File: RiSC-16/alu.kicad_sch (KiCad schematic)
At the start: 0 parts

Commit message: Added sheet for register file.
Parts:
- added C1, C2, C3, C4, C5: 0.1 uF, symbol Device:C_Small_US
- added U1: 74LS283, symbol 74xx:74LS283
- added U2: 74LS00, symbol 74xx:74LS00
- added U3, U5: 74LS175, symbol 74xx:74LS175
- added U4: 74LS257, symbol 74xx:74LS257
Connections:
- new net: U1.1 (S2), U4.5 (I0b)
- new net: U1.10 (S4), U4.11 (I0d)
- new net: U1.11 (B4), U2.13, U5.15 (Q3)
- new net: U1.12 (A4), U2.12, U3.15 (Q3)
- new net: U1.13 (S3), U4.14 (I0c)
- new net: U1.14 (A3), U2.9, U3.10 (Q2)
- new net: U1.15 (B3), U2.10, U5.10 (Q2)
- new net: U1.2 (B2), U2.5, U5.7 (Q1)
- new net: U1.3 (A2), U2.4, U3.7 (Q1)
- new net: U1.4 (S1), U4.2 (I0a)
- new net: U1.5 (A1), U2.1, U3.2 (Q0)
- new net: U1.6 (B1), U2.2, U5.2 (Q0)
- new net: U2.11, U4.10 (I1d)
- new net: U2.8, U4.13 (I1c)
- new net: U2.3, U4.3 (I1a)
- new net: U2.6, U4.6 (I1b)
- new net +5V: C1.1, C2.1, C3.1, C4.1, C5.1, U1.16 (VCC), U2.14 (VCC), U3.16 (VCC), U4.16 (VCC), U5.16 (VCC)
- new net ADD/NAND: U4.1 (S)
- new net ALUout: U4.15 (OE)
- new net Ain: U3.9 (Cp)
- new net Bin: U5.9 (Cp)
- new net Cin: U1.7 (C0)
- new net Cout: U1.9 (C4)
- new net GND: C1.2, C2.2, C3.2, C4.2, C5.2, U1.8 (GND), U2.7 (GND), U3.8 (GND), U4.8 (GND), U5.8 (GND)
- new net Reset: U3.1 (~{Mr}), U5.1 (~{Mr})
- new net d0: U3.4 (D0), U4.4 (Za), U5.4 (D0)
- new net d1: U3.5 (D1), U4.7 (Zb), U5.5 (D1)
- new net d2: U3.12 (D2), U4.12 (Zc), U5.12 (D2)
- new net d3: U3.13 (D3), U4.9 (Zd), U5.13 (D3)
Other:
- note added: "ALU 4-bit slice Four required for ALU"

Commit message: First draft of register file.
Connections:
- net d0: no longer U5.4 (D0)
- net d1: no longer U5.5 (D1)
- net d2: no longer U5.12 (D2)
- net d3: no longer U5.13 (D3)
- new net a0: U5.4 (D0)
- new net a1: U5.5 (D1)
- new net a2: U5.12 (D2)
- new net a3: U5.13 (D3)

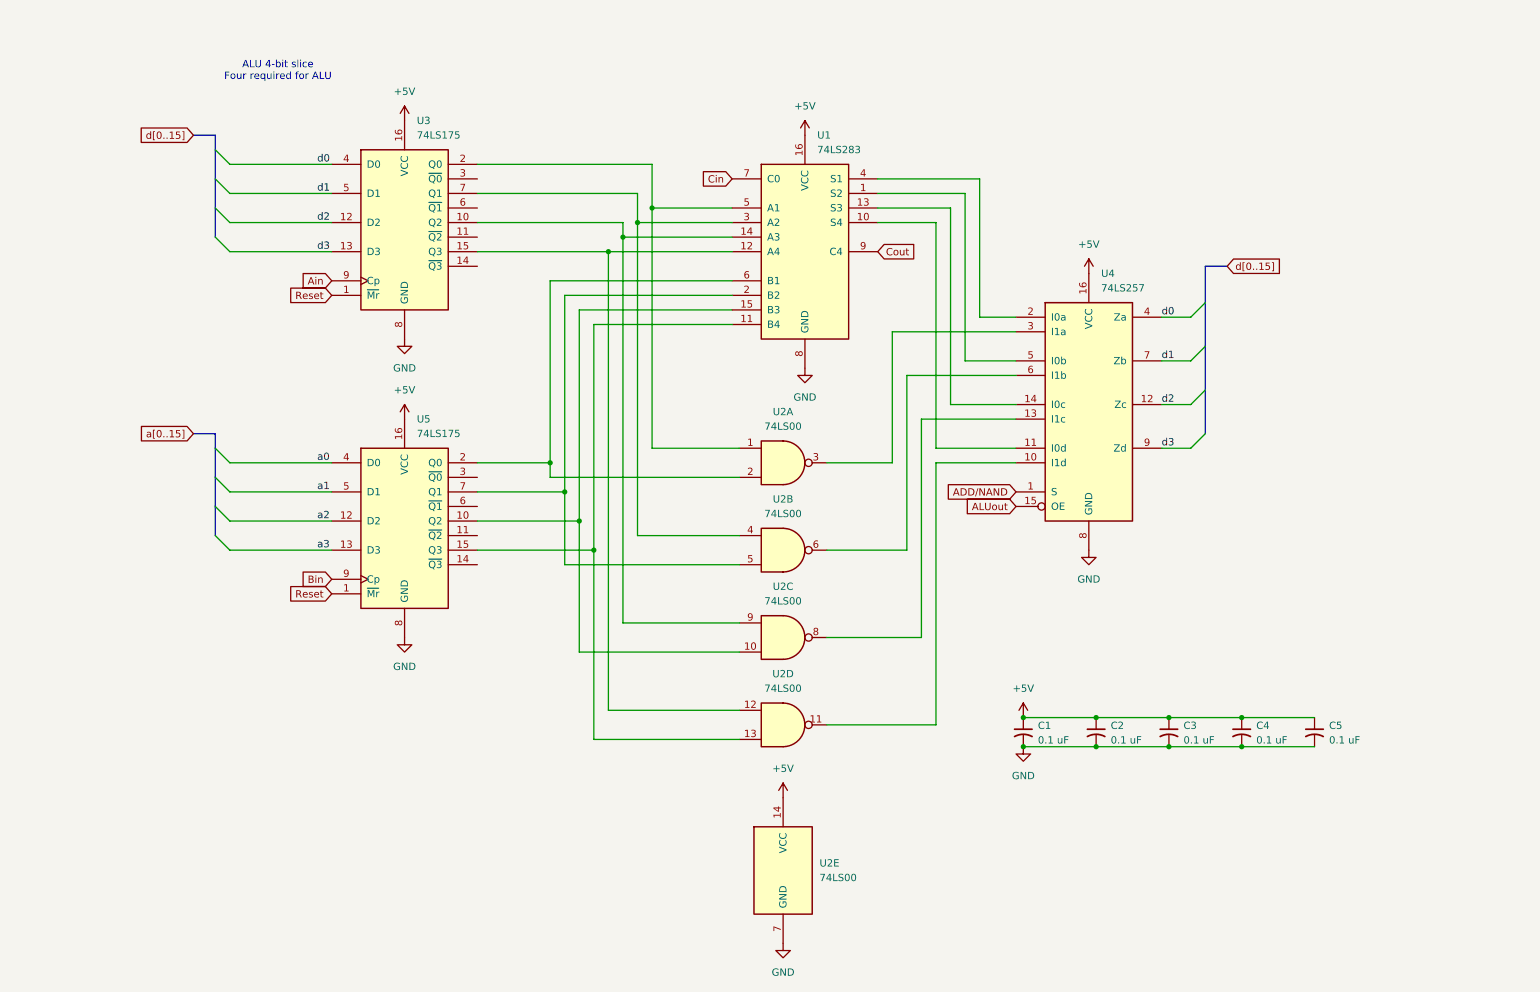
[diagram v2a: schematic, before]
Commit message: Reworked ALU to use 74LS181 and control signals from Pro. Jacob's reference paper.
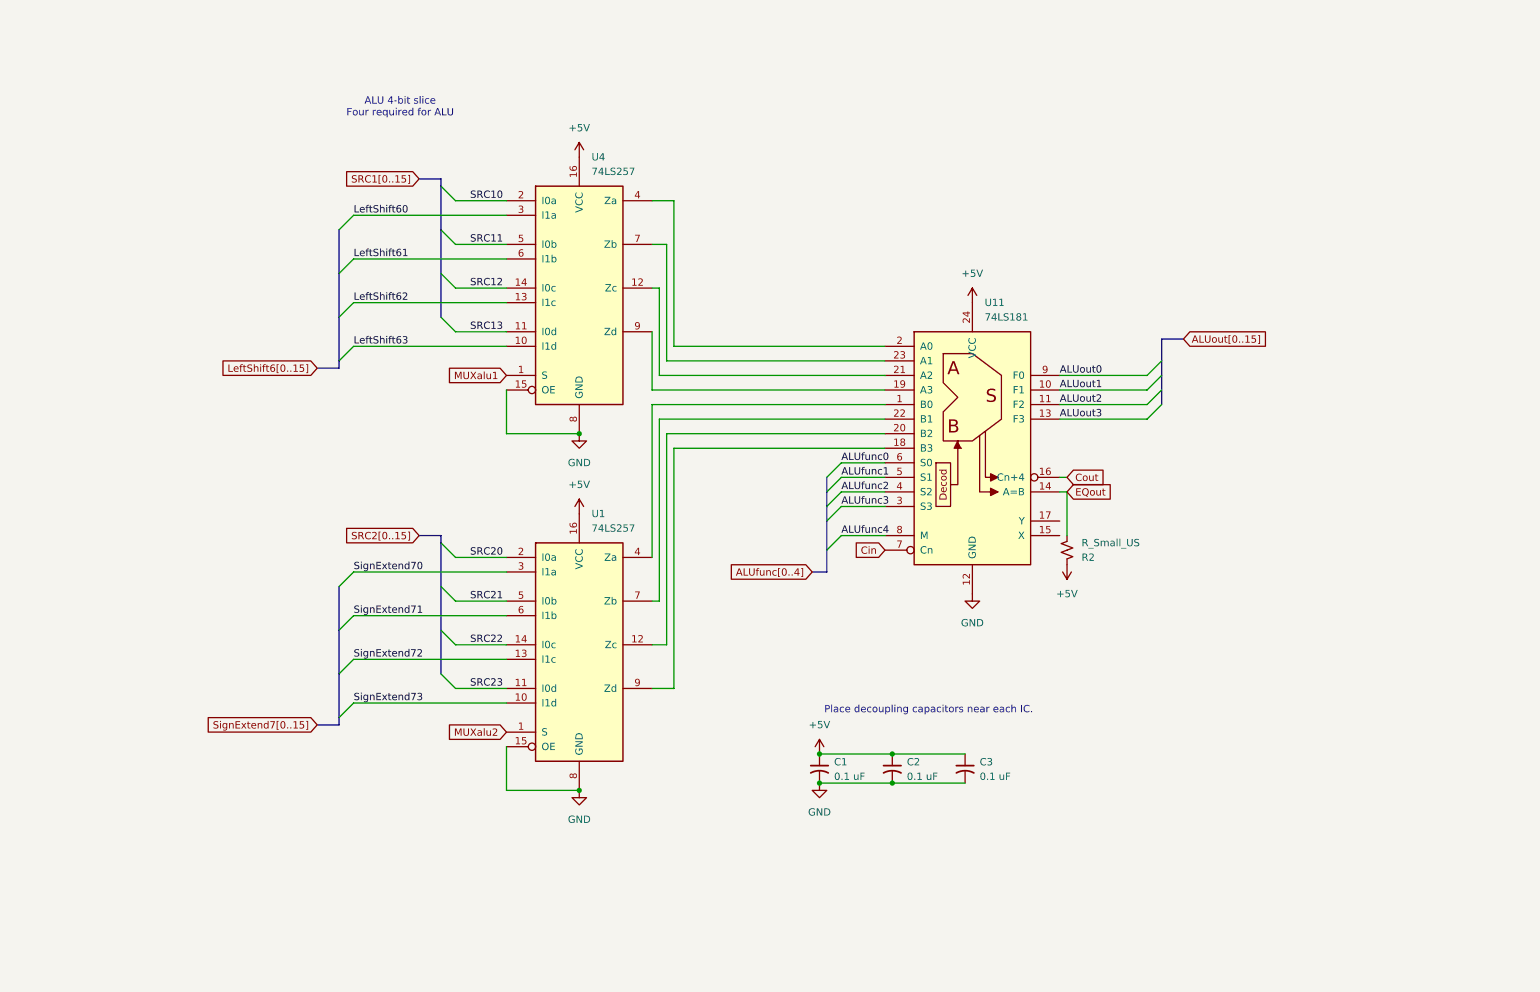
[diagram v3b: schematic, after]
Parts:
- removed C4, C5: 0.1 uF, symbol Device:C_Small_US
- removed U1: 74LS283, symbol 74xx:74LS283
- removed U2: 74LS00, symbol 74xx:74LS00
- removed U3, U5: 74LS175, symbol 74xx:74LS175
- added R2: R_Small_US, symbol Device:R_Small_US
- added U1: 74LS257, symbol 74xx:74LS257
- added U11: 74LS181, symbol 74xx:74LS181
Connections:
- net ALUout is gone; now on net GND: U4.15 (OE)
- net +5V: now also R2.1, U1.16 (VCC), U11.24 (VCC)
- net Cin: now also U11.7 (Cn)
- net Cout: now also U11.16 (Cn+4)
- net GND: now also U1.15 (OE), U1.8 (GND), U11.12 (GND)
- net SRC11: now reaches U4.5 (I0b)
- net SRC13: now reaches U4.11 (I0d)
- net SRC12: now reaches U4.14 (I0c)
- net SRC10: now reaches U4.2 (I0a)
- net LeftShift63: now reaches U4.10 (I1d)
- net LeftShift62: now reaches U4.13 (I1c)
- net LeftShift60: now reaches U4.3 (I1a)
- net LeftShift61: now reaches U4.6 (I1b)
- net ADD/NAND renamed MUXalu1
- net d0: no longer names the net of U4.4 (Za)
- net d0: now also U11.2 (A0)
- net d1: no longer names the net of U4.7 (Zb)
- net d1: now also U11.23 (A1)
- net d2: no longer names the net of U4.12 (Zc)
- net d2: now also U11.21 (A2)
- net d3: no longer names the net of U4.9 (Zd)
- net d3: now also U11.19 (A3)
- new net: U1.12 (Zc), U11.20 (B2)
- new net: U1.4 (Za), U11.1 (B0)
- new net: U1.7 (Zb), U11.22 (B1)
- new net: U1.9 (Zd), U11.18 (B3)
- new net ALUfunc0: U11.6 (S0)
- new net ALUfunc1: U11.5 (S1)
- new net ALUfunc2: U11.4 (S2)
- new net ALUfunc3: U11.3 (S3)
- new net ALUfunc4: U11.8 (M)
- new net ALUout0: U11.9 (F0)
- new net ALUout1: U11.10 (F1)
- new net ALUout2: U11.11 (F2)
- new net ALUout3: U11.13 (F3)
- new net EQout: R2.2, U11.14 (A=B)
- new net MUXalu2: U1.1 (S)
- new net SRC20: U1.2 (I0a)
- new net SRC21: U1.5 (I0b)
- new net SRC22: U1.14 (I0c)
- new net SRC23: U1.11 (I0d)
- new net SignExtend70: U1.3 (I1a)
- new net SignExtend71: U1.6 (I1b)
- new net SignExtend72: U1.13 (I1c)
- new net SignExtend73: U1.10 (I1d)
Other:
- note added: "Place decoupling capacitors near each IC."
- moved on the sheet: C1, C2, C3, U4

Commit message: Added program counter page.
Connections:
- net SignExtend71 renamed SignExt71
- net SignExtend72 renamed SignExt72
- net SignExtend73 renamed SignExt73
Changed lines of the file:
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@@
 		)
 	)
-	(label "SignExtend71"
+	(label "SignExt71"
 		(at 77.47 124.46 0)
 		(effects
@@
 		)
 	)
-	(label "SignExtend72"
+	(label "SignExt72"
 		(at 77.47 132.08 0)
 		(effects
@@
 		)
 	)
-	(label "SignExtend73"
+	(label "SignExt73"
 		(at 77.47 139.7 0)
 		(effects
@@
 		)
 	)
-	(global_label "SignExtend7[0..15]"
+	(global_label "SignExt7[0..15]"
 		(shape input)
 		(at 71.12 143.51 180)
@@
 		)
 		(property "Intersheetrefs" "${INTERSHEET_REFS}"
-			(at 49.9921 143.51 0)
-			(effects
-				(font
+			(at 53.3787 143.51 0)
+			(effects
+				(font

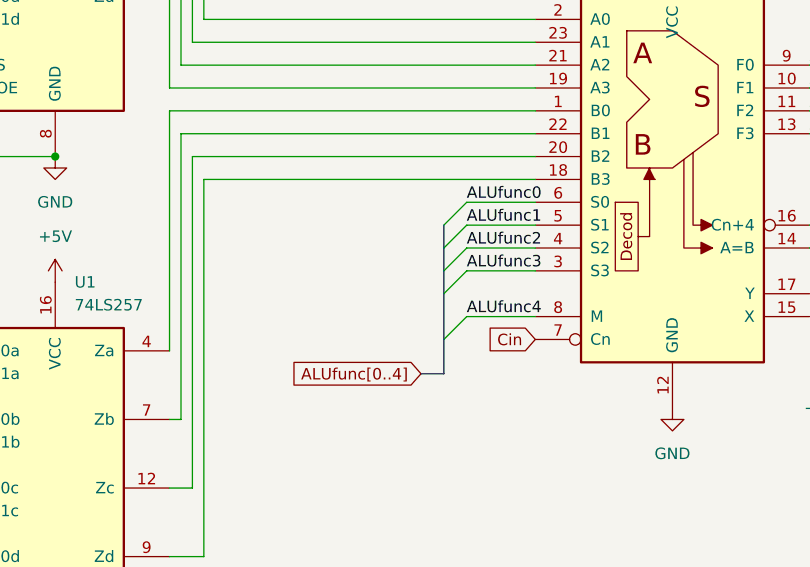
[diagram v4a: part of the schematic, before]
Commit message: Added instruction register design.
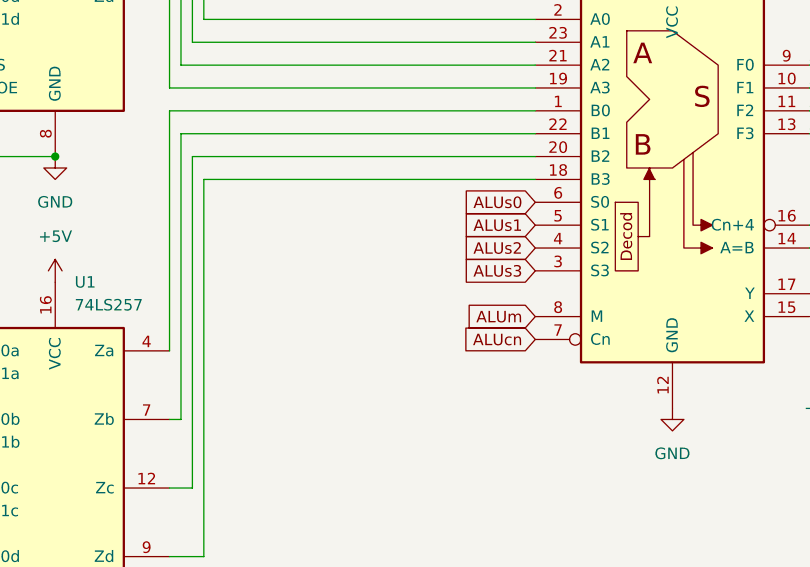
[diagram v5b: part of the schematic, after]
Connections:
- net ALUfunc0 renamed ALUs0
- net ALUfunc1 renamed ALUs1
- net ALUfunc2 renamed ALUs2
- net ALUfunc3 renamed ALUs3
- net ALUfunc4 renamed ALUm
- net Cin renamed ALUcn
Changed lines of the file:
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@@
-	)
-	(bus_entry
-		(at 160.02 113.03)
-		(size 2.54 -2.54)
-		(stroke
-			(width 0)
-			(type default)
-		)
 	)
 	(bus_entry
@@
 	)
 	(bus_entry
-		(at 160.02 105.41)
-		(size 2.54 -2.54)
-		(stroke
-			(width 0)
-			(type default)
-		)
-	)
-	(bus_entry
 		(at 74.93 119.38)
 		(size 2.54 -2.54)
@@
 	)
 	(bus_entry
-		(at 160.02 107.95)
-		(size 2.54 -2.54)
-		(stroke
-			(width 0)
-			(type default)
-		)
-	)
-	(bus_entry
 		(at 218.44 87.63)
 		(size -2.54 2.54)
@@
 	)
 	(bus_entry
-		(at 160.02 100.33)
-		(size 2.54 -2.54)
-		(stroke
-			(width 0)
-			(type default)
-		)
-	)
-	(bus_entry
 		(at 74.93 142.24)
 		(size 2.54 -2.54)
@@
 	)
 	(bus_entry
-		(at 160.02 102.87)
-		(size 2.54 -2.54)
-		(stroke
-			(width 0)
-			(type default)
-		)
-	)
-	(bus_entry
 		(at 74.93 72.39)
 		(size 2.54 -2.54)
@@
 	(bus
 		(pts
-			(xy 160.02 113.03) (xy 160.02 116.84)
-		)
-		(stroke
-			(width 0)
-			(type default)
-		)
-	)
-	(bus
-		(pts
 			(xy 74.93 64.77) (xy 74.93 72.39)
 		)
@@
 	(wire
 		(pts
-			(xy 162.56 100.33) (xy 170.18 100.33)
-		)
-		(stroke
-			(width 0)
-			(type default)
-		)
-	)
-	(wire
-		(pts
 			(xy 77.47 69.85) (xy 104.14 69.85)
 		)
@@
 	(wire
 		(pts
-			(xy 162.56 105.41) (xy 170.18 105.41)
-		)
-		(stroke
-			(width 0)
-			(type default)
-		)
-	)
-	(wire
-		(pts
 			(xy 170.18 95.25) (xy 133.35 95.25)
 		)
@@
 		)
 	)
-	(wire
-		(pts
-			(xy 162.56 97.79) (xy 170.18 97.79)
-		)
-		(stroke
-			(width 0)
-			(type default)
-		)
-	)
 	(bus
 		(pts
@@
 		)
 	)
-	(wire
-		(pts
-			(xy 162.56 110.49) (xy 170.18 110.49)
-		)
-		(stroke
-			(width 0)
-			(type default)
-		)
-	)
-	(bus
-		(pts
-			(xy 160.02 107.95) (xy 160.02 113.03)
-		)
-		(stroke
-			(width 0)
-			(type default)
-		)
-	)
 	(bus
 		(pts
@@
 		)
 	)
-	(bus
-		(pts
-			(xy 160.02 100.33) (xy 160.02 102.87)
-		)
-		(stroke
-			(width 0)
-			(type default)
-		)
-	)
 	(wire
 		(pts
@@
 		)
 	)
-	(bus
-		(pts
-			(xy 160.02 102.87) (xy 160.02 105.41)
-		)
-		(stroke
-			(width 0)
-			(type default)
-		)
-	)
 	(wire
 		(pts
@@
 	(bus
 		(pts
-			(xy 160.02 105.41) (xy 160.02 107.95)
-		)
-		(stroke
-			(width 0)
-			(type default)
-		)
-	)
-	(bus
-		(pts
 			(xy 92.71 64.77) (xy 92.71 72.39)
 		)
@@
 		(pts
 			(xy 95.25 52.07) (xy 104.14 52.07)
-		)
-		(stroke
-			(width 0)
-			(type default)
-		)
-	)
-	(bus
-		(pts
-			(xy 157.48 116.84) (xy 160.02 116.84)
-		)
-		(stroke
-			(width 0)
-			(type default)
-		)
-	)
-	(wire
-		(pts
-			(xy 162.56 102.87) (xy 170.18 102.87)
 		)
 		(stroke
@@
 		)
 	)
-	(label "ALUfunc4"
-		(at 162.56 110.49 0)
-		(effects
-			(font
-				(size 1.27 1.27)
-			)
-			(justify left bottom)
-		)
-	)
 	(label "ALUout3"
 		(at 200.66 90.17 0)
@@
 		)
 	)
-	(label "ALUfunc1"
-		(at 162.56 100.33 0)
-		(effects
-			(font
-				(size 1.27 1.27)
-			)
-			(justify left bottom)
-		)
-	)
 	(label "SRC13"
 		(at 97.79 74.93 0)
@@
 		)
 	)
-	(label "ALUfunc3"
-		(at 162.56 105.41 0)
-		(effects
-			(font
-				(size 1.27 1.27)
-			)
-			(justify left bottom)
-		)
-	)
 	(label "SRC20"
 		(at 97.79 114.3 0)
@@
 		)
 	)
-	(label "ALUfunc0"
-		(at 162.56 97.79 0)
-		(effects
-			(font
-				(size 1.27 1.27)
-			)
-			(justify left bottom)
-		)
-	)
-	(label "ALUfunc2"
-		(at 162.56 102.87 0)
-		(effects
-			(font
-				(size 1.27 1.27)
-			)
-			(justify left bottom)
-		)
-	)
 	(label "SignExt72"
 		(at 77.47 132.08 0)
@@
 			)
 			(justify left bottom)
+		)
+	)
+	(global_label "ALUs1"
+		(shape input)
+		(at 170.18 100.33 180)
+		(fields_autoplaced yes)
+		(effects
+			(font
+				(size 1.27 1.27)
+			)
+			(justify right)
+		)
+		(property "Intersheetrefs" "${INTERSHEET_REFS}"
+			(at 161.51 100.33 0)
+			(effects
+				(font
+					(size 1.27 1.27)
+				)
+				(justify right)
+				(hide yes)
+			)
 		)
 	)
@@
 		)
 	)
-	(global_label "ALUfunc[0..4]"
-		(shape input)
-		(at 157.48 116.84 180)
-		(fields_autoplaced yes)
-		(effects
-			(font
-				(size 1.27 1.27)
-			)
-			(justify right)
-		)
-		(property "Intersheetrefs" "${INTERSHEET_REFS}"
-			(at 141.6133 116.84 0)
-			(effects
-				(font
-					(size 1.27 1.27)
-				)
-				(justify right)
-				(hide yes)
-			)
-		)
-	)
 	(global_label "LeftShift6[0..15]"
 		(shape input)
@@
 		)
 	)
+	(global_label "ALUs2"
+		(shape input)
+		(at 170.18 102.87 180)
+		(fields_autoplaced yes)
+		(effects
+			(font
+				(size 1.27 1.27)
+			)
+			(justify right)
+		)
+		(property "Intersheetrefs" "${INTERSHEET_REFS}"
+			(at 161.51 102.87 0)
+			(effects
+				(font
+					(size 1.27 1.27)
+				)
+				(justify right)
+				(hide yes)
+			)
+		)
+	)
 	(global_label "MUXalu1"
 		(shape input)
@@
 		)
 	)
+	(global_label "ALUs3"
+		(shape input)
+		(at 170.18 105.41 180)
+		(fields_autoplaced yes)
+		(effects
+			(font
+				(size 1.27 1.27)
+			)
+			(justify right)
+		)
+		(property "Intersheetrefs" "${INTERSHEET_REFS}"
+			(at 161.51 105.41 0)
+			(effects
+				(font
+					(size 1.27 1.27)
+				)
+				(justify right)
+				(hide yes)
+			)
+		)
+	)
 	(global_label "ALUout[0..15]"
 		(shape input)
@@
 		)
 	)
-	(global_label "Cin"
+	(global_label "ALUs0"
 		(shape input)
-		(at 170.18 113.03 180)
+		(at 170.18 97.79 180)
 		(fields_autoplaced yes)
 		(effects
@@
 		)
 		(property "Intersheetrefs" "${INTERSHEET_REFS}"
-			(at 164.171 113.03 0)
+			(at 161.51 97.79 0)
 			(effects
 				(font
@@
 		)
 	)
+	(global_label "ALUcn"
+		(shape input)
+		(at 170.18 113.03 180)
+		(fields_autoplaced yes)
+		(effects
+			(font
+				(size 1.27 1.27)
+			)
+			(justify right)
+		)
+		(property "Intersheetrefs" "${INTERSHEET_REFS}"
+			(at 161.51 113.03 0)
+			(effects
+				(font
+					(size 1.27 1.27)
+				)
+				(justify right)
+				(hide yes)
+			)
+		)
+	)
 	(global_label "SRC2[0..15]"
 		(shape input)
@@
 			(effects
 				(font
+					(size 1.27 1.27)
+				)
+				(justify right)
+				(hide yes)
+			)
+		)
+	)
+	(global_label "ALUm"
+		(shape input)
+		(at 170.18 110.49 180)
+		(fields_autoplaced yes)
+		(effects
+			(font
+				(size 1.27 1.27)
+			)
+			(justify right)
+		)
+		(property "Intersheetrefs" "${INTERSHEET_REFS}"
+			(at 162.0543 110.49 0)
+			(effects
+				(font
